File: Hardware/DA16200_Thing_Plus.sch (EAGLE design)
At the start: 65 parts, among them J2 THING_PLUS, J3 Qwiic, J5 USB C, J6 microSD, J7 CORTEX_JTAG_DEBUG_PTH_NS, Q1 20V/4.2A/52mΩ/1.4W, U1 DA16200MOD, U2 CH340E_MSOP10, U3 MCP73831, U5 4MB Flash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

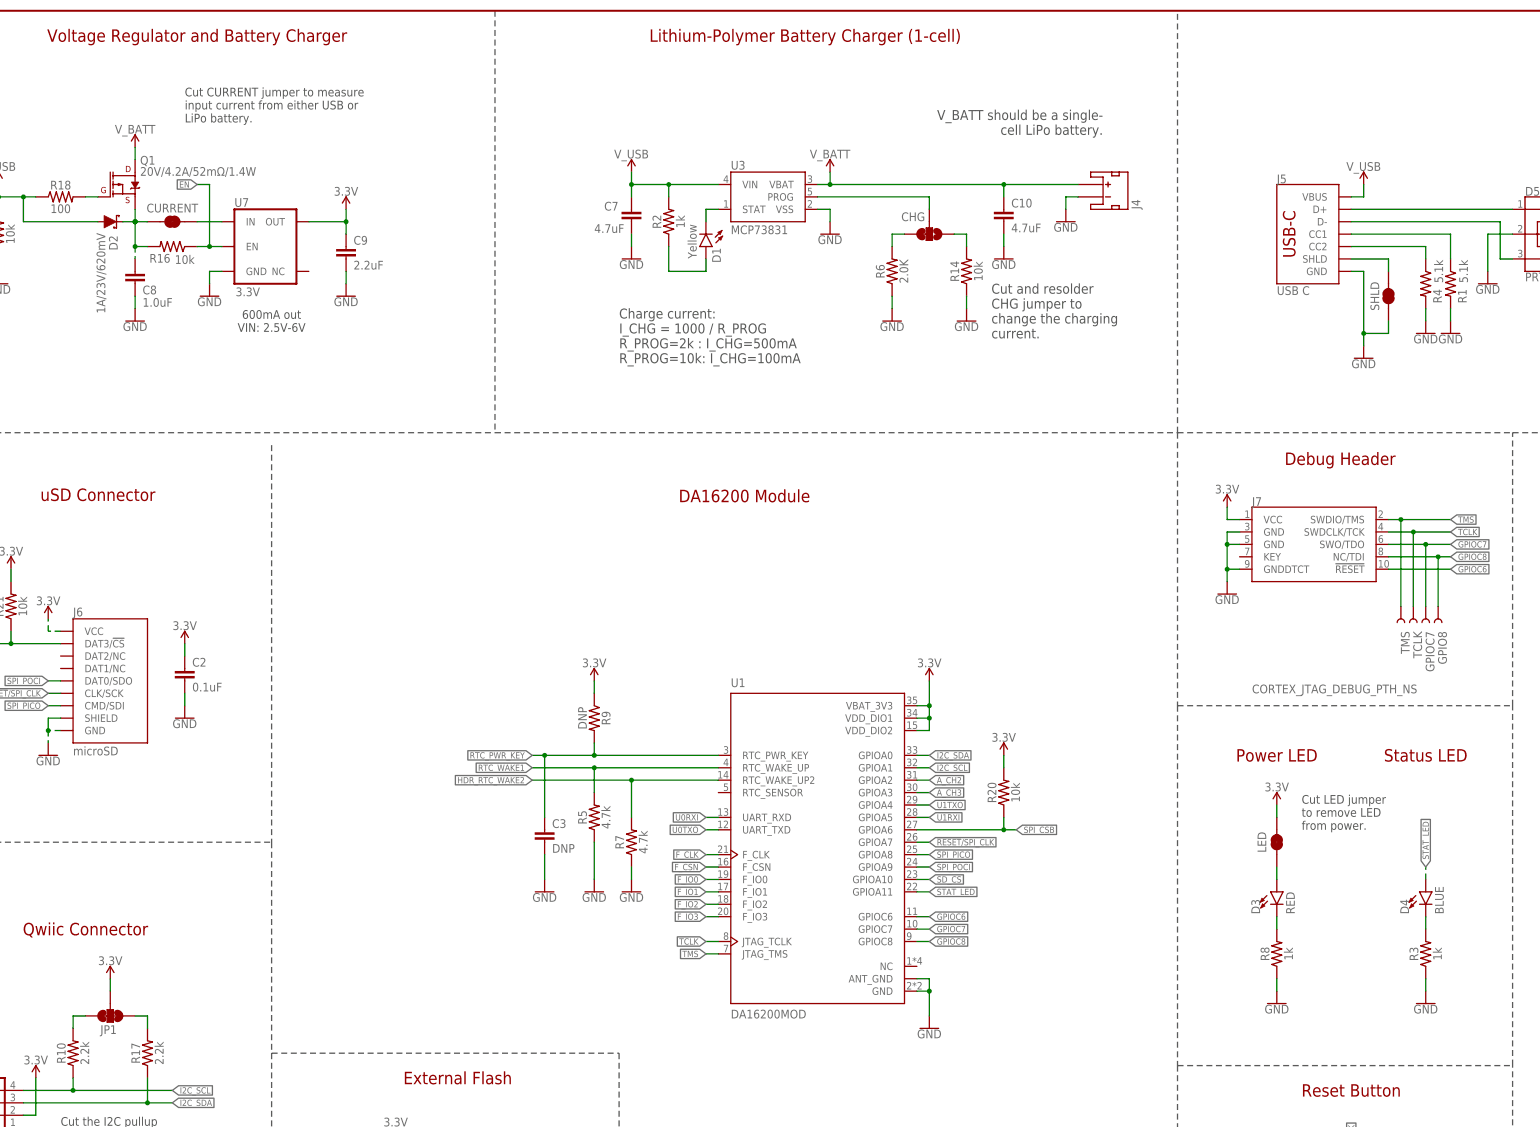
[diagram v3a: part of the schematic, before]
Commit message: QC Double-check updates
* CURR jumper to MEAS
* Move TPs onto 0.1 grid
* line up LEDs
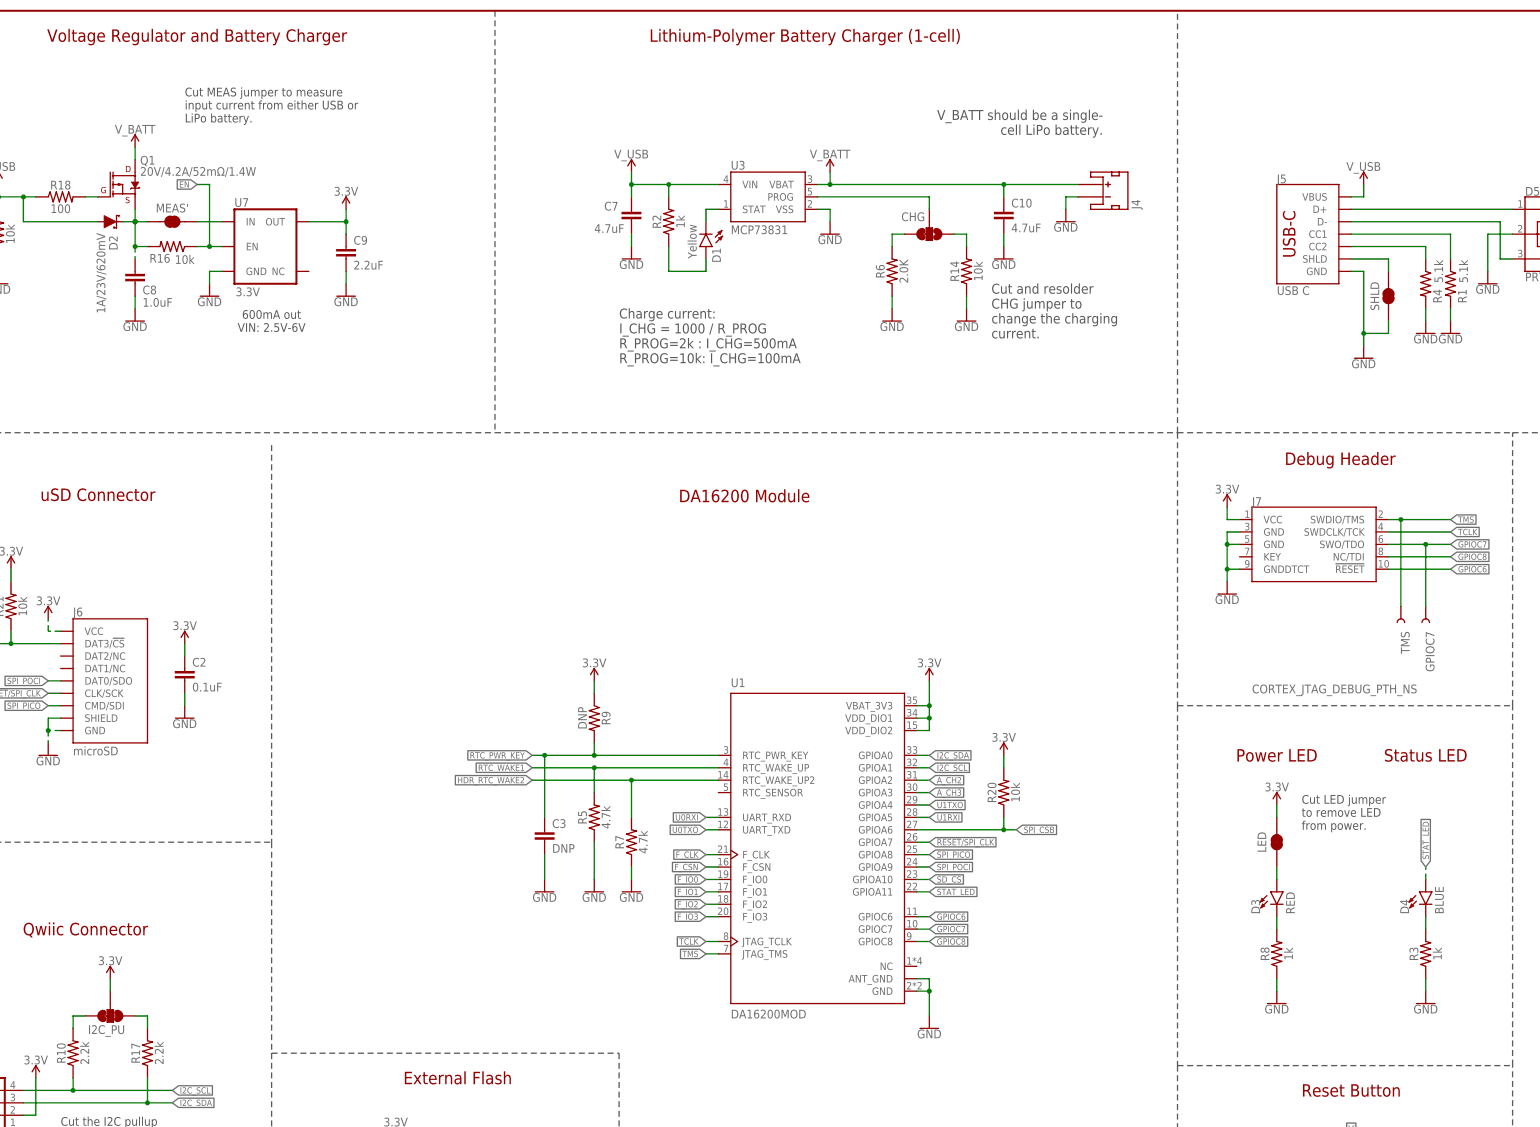
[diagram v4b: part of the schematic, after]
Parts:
- removed GPIO8, TCLK: TEST-POINT3, SparkFun-Connectors:TEST-POINT3
- renumbered CURRENT to MEAS', JP1 to I2C_PU
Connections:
- net GPIOC8: no longer GPIO8.1
- net TCLK: no longer TCLK.1
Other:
- note added: "Cut MEAS jumper to measure input current from either USB or LiPo battery."
- note removed: "Cut CURRENT jumper to measure input current from either USB or LiPo battery."
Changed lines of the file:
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@@
 <part name="FD4" library="SparkFun-Aesthetics" deviceset="FIDUCIAL" device="UFIDUCIAL" value="FIDUCIALUFIDUCIAL"/>
 <part name="J4" library="SparkFun-Connectors" deviceset="JST_2MM_MALE" device=""/>
-<part name="JP1" library="SparkFun-Jumpers" deviceset="JUMPER-SMT_3_2-NC_TRACE" device="_SILK" package3d_urn="urn:adsk.eagle:package:39289/1"/>
+<part name="I2C_PU" library="SparkFun-Jumpers" deviceset="JUMPER-SMT_3_2-NC_TRACE" device="_SILK" package3d_urn="urn:adsk.eagle:package:39289/1"/>
 <part name="H3" library="SparkFun-Hardware" deviceset="STAND-OFF" device=""/>
 <part name="H4" library="SparkFun-Hardware" deviceset="STAND-OFF" device=""/>
@@
 <part name="SUPPLY17" library="SparkFun-PowerSymbols" deviceset="3.3V" device=""/>
 <part name="GND26" library="SparkFun-PowerSymbols" deviceset="GND" device=""/>
-<part name="CURRENT" library="SparkFun-Jumpers" deviceset="JUMPER-COMBO_2_NC_TRACE" device=""/>
+<part name="MEAS'" library="SparkFun-Jumpers" deviceset="JUMPER-COMBO_2_NC_TRACE" device=""/>
 <part name="LOGO1" library="SparkFun-Aesthetics" deviceset="OSHW-LOGO" device="S"/>
 <part name="LOGO2" library="SparkFun-Aesthetics" deviceset="SFE_LOGO_NAME_FLAME" device=".1_INCH" value="SFE_LOGO_NAME_FLAME.1_INCH"/>
@@
 <part name="SUPPLY19" library="SparkFun-PowerSymbols" deviceset="3.3V" device=""/>
 <part name="TMS" library="SparkFun-Connectors" deviceset="TEST-POINT" device="3"/>
-<part name="TCLK" library="SparkFun-Connectors" deviceset="TEST-POINT" device="3"/>
 <part name="GPIOC7" library="SparkFun-Connectors" deviceset="TEST-POINT" device="3"/>
-<part name="GPIO8" library="SparkFun-Connectors" deviceset="TEST-POINT" device="3"/>
 </parts>
 <sheets>
@@
 <text x="106.68" y="45.72" size="1.778" layer="97" font="vector">Close WP jumper to
 enable write protection.</text>
-<text x="58.42" y="256.54" size="1.778" layer="97" font="vector">Cut CURRENT jumper to measure
+<text x="58.42" y="256.54" size="1.778" layer="97" font="vector">Cut MEAS jumper to measure
 input current from either USB or
 LiPo battery.</text>
@@
 <attribute name="NAME" x="252.222" y="238.76" size="1.778" layer="95" rot="MR90"/>
 </instance>
-<instance part="JP1" gate="G$1" x="43.18" y="73.66" smashed="yes" rot="R270">
-<attribute name="NAME" x="41.148" y="69.977" size="1.778" layer="95" font="vector"/>
+<instance part="I2C_PU" gate="G$1" x="43.18" y="73.66" smashed="yes" rot="R270">
+<attribute name="NAME" x="38.608" y="69.977" size="1.778" layer="95" font="vector"/>
 </instance>
 <instance part="H3" gate="G$1" x="429.26" y="33.02" smashed="yes"/>
@@
 <attribute name="VALUE" x="96.52" y="9.906" size="1.778" layer="96" align="top-center"/>
 </instance>
-<instance part="CURRENT" gate="JP1" x="55.88" y="236.22" smashed="yes">
+<instance part="MEAS'" gate="JP1" x="55.88" y="236.22" smashed="yes">
 <attribute name="NAME" x="55.88" y="239.014" size="1.778" layer="95" font="vector" align="center"/>
 </instance>
@@
 <attribute name="NAME" x="307.34" y="152.4" size="1.778" layer="95" font="vector" rot="R270"/>
 </instance>
-<instance part="TCLK" gate="G$1" x="309.88" y="157.48" smashed="yes" rot="R270">
-<attribute name="NAME" x="309.88" y="152.4" size="1.778" layer="95" font="vector" rot="R270"/>
-</instance>
 <instance part="GPIOC7" gate="G$1" x="312.42" y="157.48" smashed="yes" rot="R270">
 <attribute name="NAME" x="312.42" y="152.4" size="1.778" layer="95" font="vector" rot="R270"/>
-</instance>
-<instance part="GPIO8" gate="G$1" x="314.96" y="157.48" smashed="yes" rot="R270">
-<attribute name="NAME" x="314.96" y="152.4" size="1.778" layer="95" font="vector" rot="R270"/>
 </instance>
 </instances>
@@
 </segment>
 <segment>
-<pinref part="JP1" gate="G$1" pin="2"/>
+<pinref part="I2C_PU" gate="G$1" pin="2"/>
 <wire x1="43.18" y1="78.74" x2="43.18" y2="81.28" width="0.1524" layer="91"/>
 <pinref part="SUPPLY15" gate="G$1" pin="3.3V"/>
@@
 <segment>
 <wire x1="35.56" y1="71.12" x2="35.56" y2="73.66" width="0.1524" layer="91"/>
-<pinref part="JP1" gate="G$1" pin="3"/>
+<pinref part="I2C_PU" gate="G$1" pin="3"/>
 <wire x1="35.56" y1="73.66" x2="38.1" y2="73.66" width="0.1524" layer="91"/>
 <pinref part="R10" gate="G$1" pin="2"/>
@@
 <net name="N$3" class="0">
 <segment>
-<pinref part="JP1" gate="G$1" pin="1"/>
+<pinref part="I2C_PU" gate="G$1" pin="1"/>
 <wire x1="48.26" y1="73.66" x2="50.8" y2="73.66" width="0.1524" layer="91"/>
 <wire x1="50.8" y1="73.66" x2="50.8" y2="71.12" width="0.1524" layer="91"/>
@@
 <pinref part="R16" gate="G$1" pin="2"/>
 <pinref part="C8" gate="G$1" pin="1"/>
-<pinref part="CURRENT" gate="JP1" pin="1"/>
+<pinref part="MEAS'" gate="JP1" pin="1"/>
 <wire x1="48.26" y1="236.22" x2="50.8" y2="236.22" width="0.1524" layer="91"/>
 </segment>
@@
 <segment>
 <pinref part="J7" gate="J1" pin="NC/TDI"/>
-<wire x1="304.8" y1="167.64" x2="314.96" y2="167.64" width="0.1524" layer="91"/>
+<wire x1="304.8" y1="167.64" x2="317.5" y2="167.64" width="0.1524" layer="91"/>
 <label x="317.5" y="167.64" size="1.27" layer="95" xref="yes"/>
-<pinref part="GPIO8" gate="G$1" pin="1"/>
-<wire x1="314.96" y1="167.64" x2="317.5" y2="167.64" width="0.1524" layer="91"/>
-<wire x1="314.96" y1="157.48" x2="314.96" y2="167.64" width="0.1524" layer="91"/>
-<junction x="314.96" y="167.64"/>
 </segment>
 </net>
@@
 <segment>
 <pinref part="J7" gate="J1" pin="SWDCLK/TCK"/>
-<wire x1="304.8" y1="172.72" x2="309.88" y2="172.72" width="0.1524" layer="91"/>
 <label x="317.5" y="172.72" size="1.27" layer="95" xref="yes"/>
-<pinref part="TCLK" gate="G$1" pin="1"/>
-<wire x1="309.88" y1="172.72" x2="317.5" y2="172.72" width="0.1524" layer="91"/>
-<wire x1="309.88" y1="157.48" x2="309.88" y2="172.72" width="0.1524" layer="91"/>
-<junction x="309.88" y="172.72"/>
+<wire x1="304.8" y1="172.72" x2="317.5" y2="172.72" width="0.1524" layer="91"/>
 </segment>
 <segment>
@@
 <net name="N$22" class="0">
 <segment>
-<pinref part="CURRENT" gate="JP1" pin="2"/>
+<pinref part="MEAS'" gate="JP1" pin="2"/>
 <pinref part="U7" gate="G$1" pin="IN"/>
 <wire x1="60.96" y1="236.22" x2="66.04" y2="236.22" width="0.1524" layer="91"/>

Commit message: Updated a few parts
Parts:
- C2: device SparkFun-Capacitors:0.1UF-0402T-6.3V-10%-X7R -> SparkFun-Capacitors:0.1UF-0402T-16V-10%
- R19: value 10K -> 10k; device SparkFun-Resistors:10KOHM-0402-1/10W-0.1% -> SparkFun-Resistors:10KOHM-0402-1/16W-1%
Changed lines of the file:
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@@
 <?xml version="1.0" encoding="utf-8"?>
 <!DOCTYPE eagle SYSTEM "eagle.dtd">
-<eagle version="9.4.2">
+<eagle version="9.5.2">
 <drawing>
 <settings>
-<setting alwaysvectorfont="yes"/>
+<setting alwaysvectorfont="no"/>
 <setting keepoldvectorfont="yes"/>
 <setting verticaltext="up"/>
@@
 <part name="SUPPLY2" library="SparkFun-PowerSymbols" deviceset="3.3V" device=""/>
 <part name="GND2" library="SparkFun-PowerSymbols" deviceset="GND" device=""/>
-<part name="C2" library="SparkFun-Capacitors" deviceset="0.1UF" device="-0402T-6.3V-10%-X7R" value="0.1uF"/>
+<part name="C2" library="SparkFun-Capacitors" deviceset="0.1UF" device="-0402T-16V-10%" value="0.1uF"/>
 <part name="SUPPLY3" library="SparkFun-PowerSymbols" deviceset="3.3V" device=""/>
 <part name="GND28" library="SparkFun-PowerSymbols" deviceset="GND" device=""/>
@@
 <part name="GND25" library="SparkFun-PowerSymbols" deviceset="GND" device=""/>
 <part name="SUPPLY16" library="SparkFun-PowerSymbols" deviceset="3.3V" device=""/>
-<part name="R19" library="SparkFun-Resistors" deviceset="10KOHM" device="-0402-1/10W-0.1%" value="10K"/>
+<part name="R19" library="SparkFun-Resistors" deviceset="10KOHM" device="-0402-1/16W-1%" value="10k"/>
 <part name="WP" library="SparkFun-Jumpers" deviceset="JUMPER-SMT_2_NO" device="_SILK" package3d_urn="urn:adsk.eagle:package:39279/1"/>
 <part name="SUPPLY17" library="SparkFun-PowerSymbols" deviceset="3.3V" device=""/>

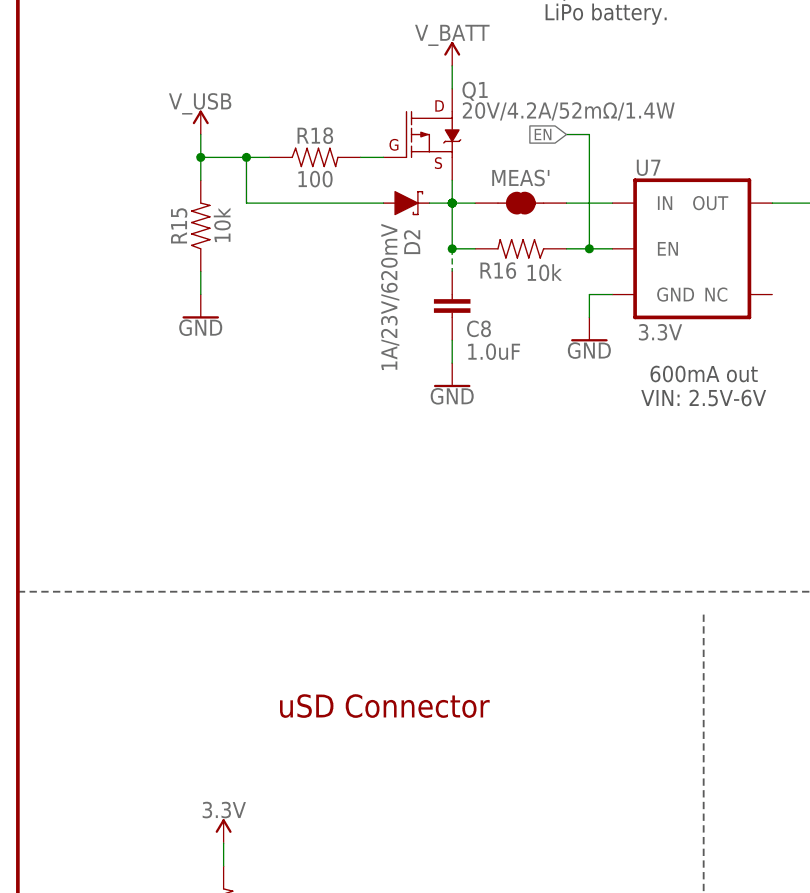
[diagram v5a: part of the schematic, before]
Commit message: Fix some names on schematic
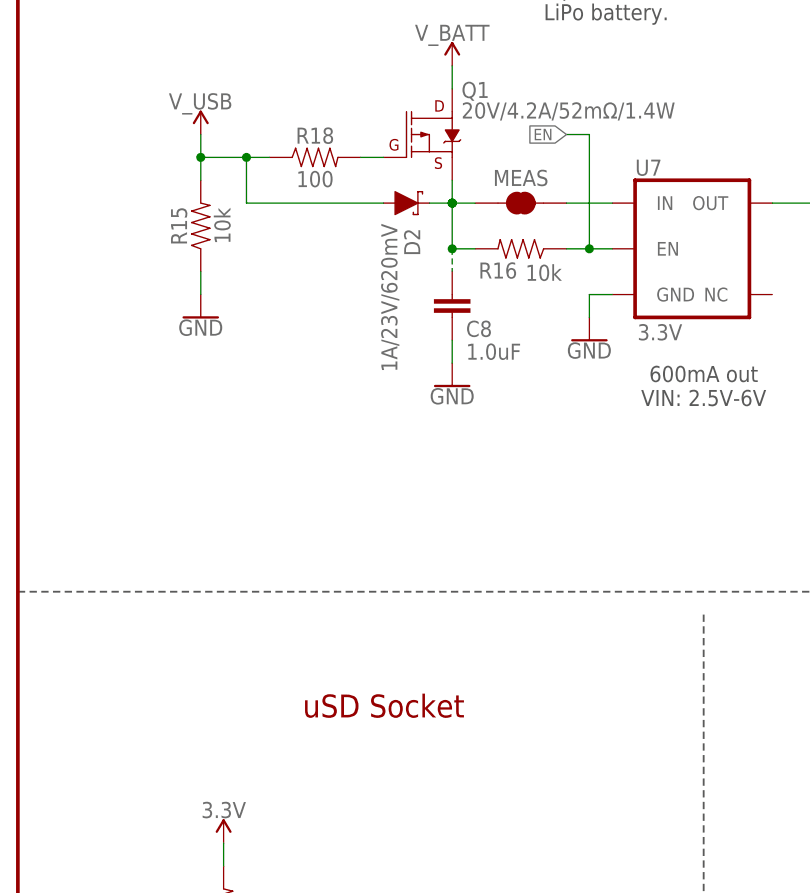
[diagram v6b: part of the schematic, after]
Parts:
- renumbered MEAS' to MEAS
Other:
- note added: "uSD Socket"
- note removed: "uSD Connector"
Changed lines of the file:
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@@
 <?xml version="1.0" encoding="utf-8"?>
 <!DOCTYPE eagle SYSTEM "eagle.dtd">
-<eagle version="9.5.2">
+<eagle version="9.4.2">
 <drawing>
 <settings>
-<setting alwaysvectorfont="no"/>
+<setting alwaysvectorfont="yes"/>
 <setting keepoldvectorfont="yes"/>
 <setting verticaltext="up"/>
@@
 <part name="SUPPLY17" library="SparkFun-PowerSymbols" deviceset="3.3V" device=""/>
 <part name="GND26" library="SparkFun-PowerSymbols" deviceset="GND" device=""/>
-<part name="MEAS'" library="SparkFun-Jumpers" deviceset="JUMPER-COMBO_2_NC_TRACE" device=""/>
+<part name="MEAS" library="SparkFun-Jumpers" deviceset="JUMPER-COMBO_2_NC_TRACE" device=""/>
 <part name="LOGO1" library="SparkFun-Aesthetics" deviceset="OSHW-LOGO" device="S"/>
 <part name="LOGO2" library="SparkFun-Aesthetics" deviceset="SFE_LOGO_NAME_FLAME" device=".1_INCH" value="SFE_LOGO_NAME_FLAME.1_INCH"/>
@@
 <wire x1="330.2" y1="137.16" x2="330.2" y2="193.04" width="0.2032" layer="97" style="longdash"/>
 <wire x1="121.92" y1="193.04" x2="261.62" y2="193.04" width="0.1524" layer="97" style="longdash"/>
-<text x="40.64" y="180.34" size="2.54" layer="94" font="vector" align="center">uSD Connector</text>
+<text x="40.64" y="180.34" size="2.54" layer="94" font="vector" align="center">uSD Socket</text>
 <wire x1="261.62" y1="193.04" x2="261.62" y2="279.4" width="0.2032" layer="97" style="longdash"/>
 <text x="294.894" y="187.706" size="2.54" layer="94" font="vector" align="center">Debug Header</text>
@@
 <attribute name="VALUE" x="96.52" y="9.906" size="1.778" layer="96" align="top-center"/>
 </instance>
-<instance part="MEAS'" gate="JP1" x="55.88" y="236.22" smashed="yes">
+<instance part="MEAS" gate="JP1" x="55.88" y="236.22" smashed="yes">
 <attribute name="NAME" x="55.88" y="239.014" size="1.778" layer="95" font="vector" align="center"/>
 </instance>
@@
 <pinref part="R16" gate="G$1" pin="2"/>
 <pinref part="C8" gate="G$1" pin="1"/>
-<pinref part="MEAS'" gate="JP1" pin="1"/>
+<pinref part="MEAS" gate="JP1" pin="1"/>
 <wire x1="48.26" y1="236.22" x2="50.8" y2="236.22" width="0.1524" layer="91"/>
 </segment>
@@
 <net name="N$22" class="0">
 <segment>
-<pinref part="MEAS'" gate="JP1" pin="2"/>
+<pinref part="MEAS" gate="JP1" pin="2"/>
 <pinref part="U7" gate="G$1" pin="IN"/>
 <wire x1="60.96" y1="236.22" x2="66.04" y2="236.22" width="0.1524" layer="91"/>
